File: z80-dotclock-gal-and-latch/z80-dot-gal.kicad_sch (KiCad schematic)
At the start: 14 parts, among them J1 Board corner fix, J2 EXP_PORT, J3 GAL_1_9, J4 GAL_11_19, U1 Z80CPU SOCKET, U2 Z80CPU, U3 74LS74, U4 GAL22V10

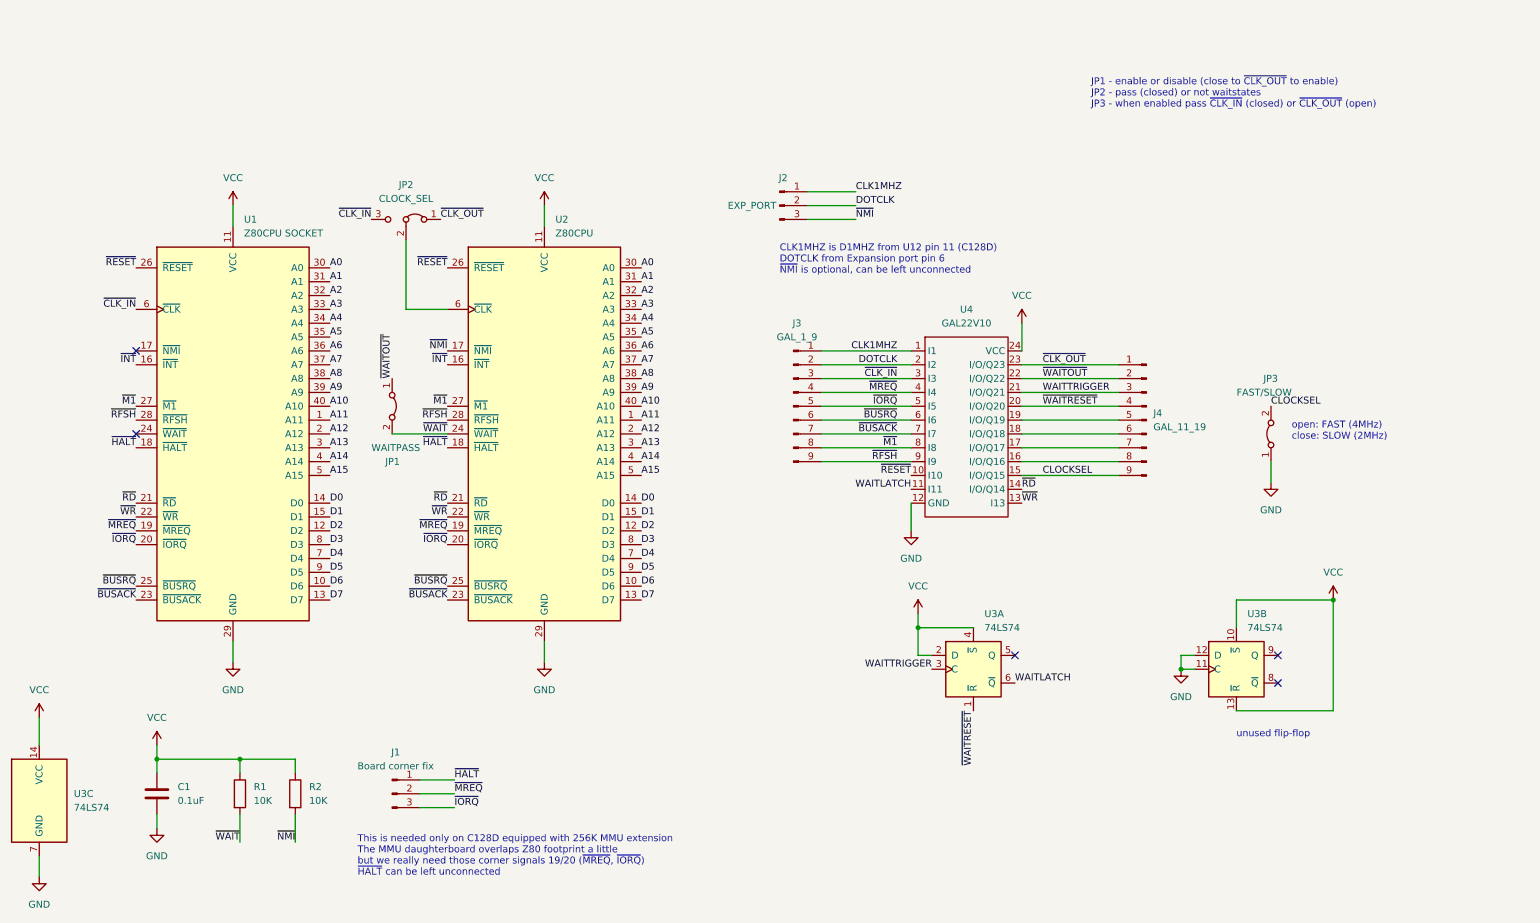
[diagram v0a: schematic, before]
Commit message: Schematic revision v2, without PCB: - remove test pads - remove unused connections to GAL pins 6-8 - add J3 and lots of descriptions - add required connects to /WR, /RESET, /RFSH - make GAL socket compatible with 16V8
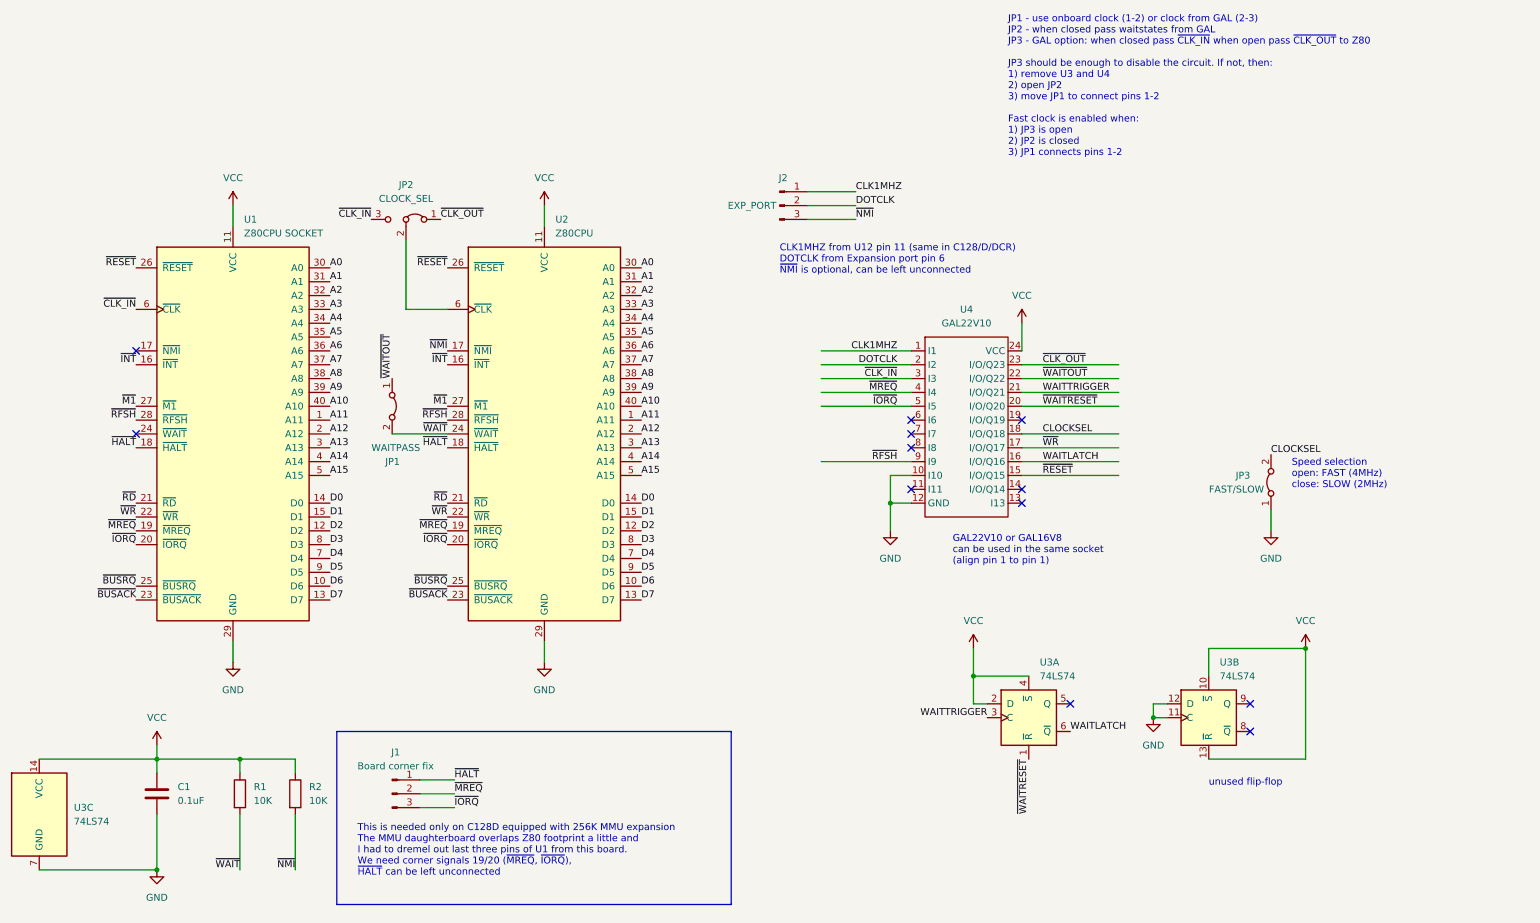
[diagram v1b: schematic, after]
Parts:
- removed J3: GAL_1_9, Connector_PinHeader_2.54mm:PinHeader_1x09_P2.54mm_Vertical, symbol Connector:Conn_01x09_Male
- removed J4: GAL_11_19, Connector_PinHeader_2.54mm:PinHeader_1x09_P2.54mm_Vertical, symbol Connector:Conn_01x09_Male
- U3: footprint (none) -> Package_DIP:DIP-14_W7.62mm_Socket
- U4: footprint (none) -> Package_DIP:DIP-24_W7.62mm_Socket
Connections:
- net CLOCKSEL: now also U4.18 (I/O/Q18); no longer U4.15 (I/O/Q15)
- net GND: now also U4.10 (I10)
- net WAITLATCH: now also U4.16 (I/O/Q16); no longer U4.11 (I11)
- net ~{BUSACK}: no longer U4.7 (I7)
- net ~{BUSRQ}: no longer U4.6 (I6)
- net ~{M1}: no longer U4.8 (I8)
- net ~{RD}: no longer U4.14 (I/O/Q14)
- net ~{RESET}: now also U4.15 (I/O/Q15); no longer U4.10 (I10)
- net ~{WR}: now also U4.17 (I/O/Q17); no longer U4.13 (I13)
- no-connect marks 5 -> 12
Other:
- note added: "CLK1MHZ from U12 pin 11 (same in C128/D/DCR) DOTCLK from Expansion port pin 6 ~{NMI} is optional, can be left unconnected"
- note added: "GAL22V10 or GAL16V8 can be used in the same socket (align pin 1 to pin 1)"
- note added: "JP1 - use onboard clock (1-2) or clock from GAL (2-3) JP2 - when closed pass waitstates from GAL JP3 - GAL option: when closed pass ~{CLK_IN} when open pass ~{CLK_OUT} to Z80 JP3 should be enough to disable the circuit. If not, then: 1) remove U3 and U4 2) open JP2 3) move JP1 to connect pins 1-2 Fast clock is enabled when: 1) JP3 is open 2) JP2 is closed 3) JP1 connects pins 1-2"
- note added: "Speed selection open: FAST (4MHz) close: SLOW (2MHz)"
- note added: "This is needed only on C128D equipped with 256K MMU expansion The MMU daughterboard overlaps Z80 footprint a little and I had to dremel out last three pins of U1 from this board. We need corner signals 19/20 (~{MREQ}, ~{IORQ}), ~{HALT} can be left unconnected"
- note removed: "CLK1MHZ is D1MHZ from U12 pin 11 (C128D) DOTCLK from Expansion port pin 6 ~{NMI} is optional, can be left unconnected"
- note removed: "JP1 - enable or disable (close to ~{CLK_OUT} to enable) JP2 - pass (closed) or not waitstates JP3 - when enabled pass ~{CLK_IN} (closed) or ~{CLK_OUT} (open)"
- note removed: "This is needed only on C128D equipped with 256K MMU extension The MMU daughterboard overlaps Z80 footprint a little but we really need those corner signals 19/20 (~{MREQ}, ~{IORQ}) ~{HALT} can be left unconnected"
- note removed: "open: FAST (4MHz) close: SLOW (2MHz)"
- moved on the sheet: JP3, U3A, U3B, U3C

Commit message: correct descriptions
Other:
- note added: "JP1 - when closed pass waitstates from GAL JP2 - use onboard clock (1-2) or clock from GAL (2-3) JP3 - GAL option: when closed pass ~{CLK_IN} when open pass ~{CLK_OUT} to Z80 JP3 should be enough to disable the circuit. If not, then: 1) remove U3 and U4 2) move JP2 to connect pins 1-2 3) open JP1 Fast clock is enabled when: 1) JP3 is open 2) JP2 connects pins 1-2 3) JP1 is closed"
- note removed: "JP1 - use onboard clock (1-2) or clock from GAL (2-3) JP2 - when closed pass waitstates from GAL JP3 - GAL option: when closed pass ~{CLK_IN} when open pass ~{CLK_OUT} to Z80 JP3 should be enough to disable the circuit. If not, then: 1) remove U3 and U4 2) open JP2 3) move JP1 to connect pins 1-2 Fast clock is enabled when: 1) JP3 is open 2) JP2 is closed 3) JP1 connects pins 1-2"
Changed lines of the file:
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@@
     (effects (font (size 1.27 1.27)) (justify left bottom))
   )
-  (text "JP1 - use onboard clock (1-2) or clock from GAL (2-3)\nJP2 - when closed pass waitstates from GAL\nJP3 - GAL option: when closed pass ~{CLK_IN} when open pass ~{CLK_OUT} to Z80\n\nJP3 should be enough to disable the circuit. If not, then:\n1) remove U3 and U4\n2) open JP2\n3) move JP1 to connect pins 1-2\n\nFast clock is enabled when:\n1) JP3 is open\n2) JP2 is closed\n3) JP1 connects pins 1-2\n"
+  (text "JP1 - when closed pass waitstates from GAL\nJP2 - use onboard clock (1-2) or clock from GAL (2-3)\nJP3 - GAL option: when closed pass ~{CLK_IN} when open pass ~{CLK_OUT} to Z80\n\nJP3 should be enough to disable the circuit. If not, then:\n1) remove U3 and U4\n2) move JP2 to connect pins 1-2\n3) open JP1\n\nFast clock is enabled when:\n1) JP3 is open\n2) JP2 connects pins 1-2\n3) JP1 is closed\n"
     (at 201.93 41.91 0)
     (effects (font (size 1.27 1.27)) (justify left bottom))

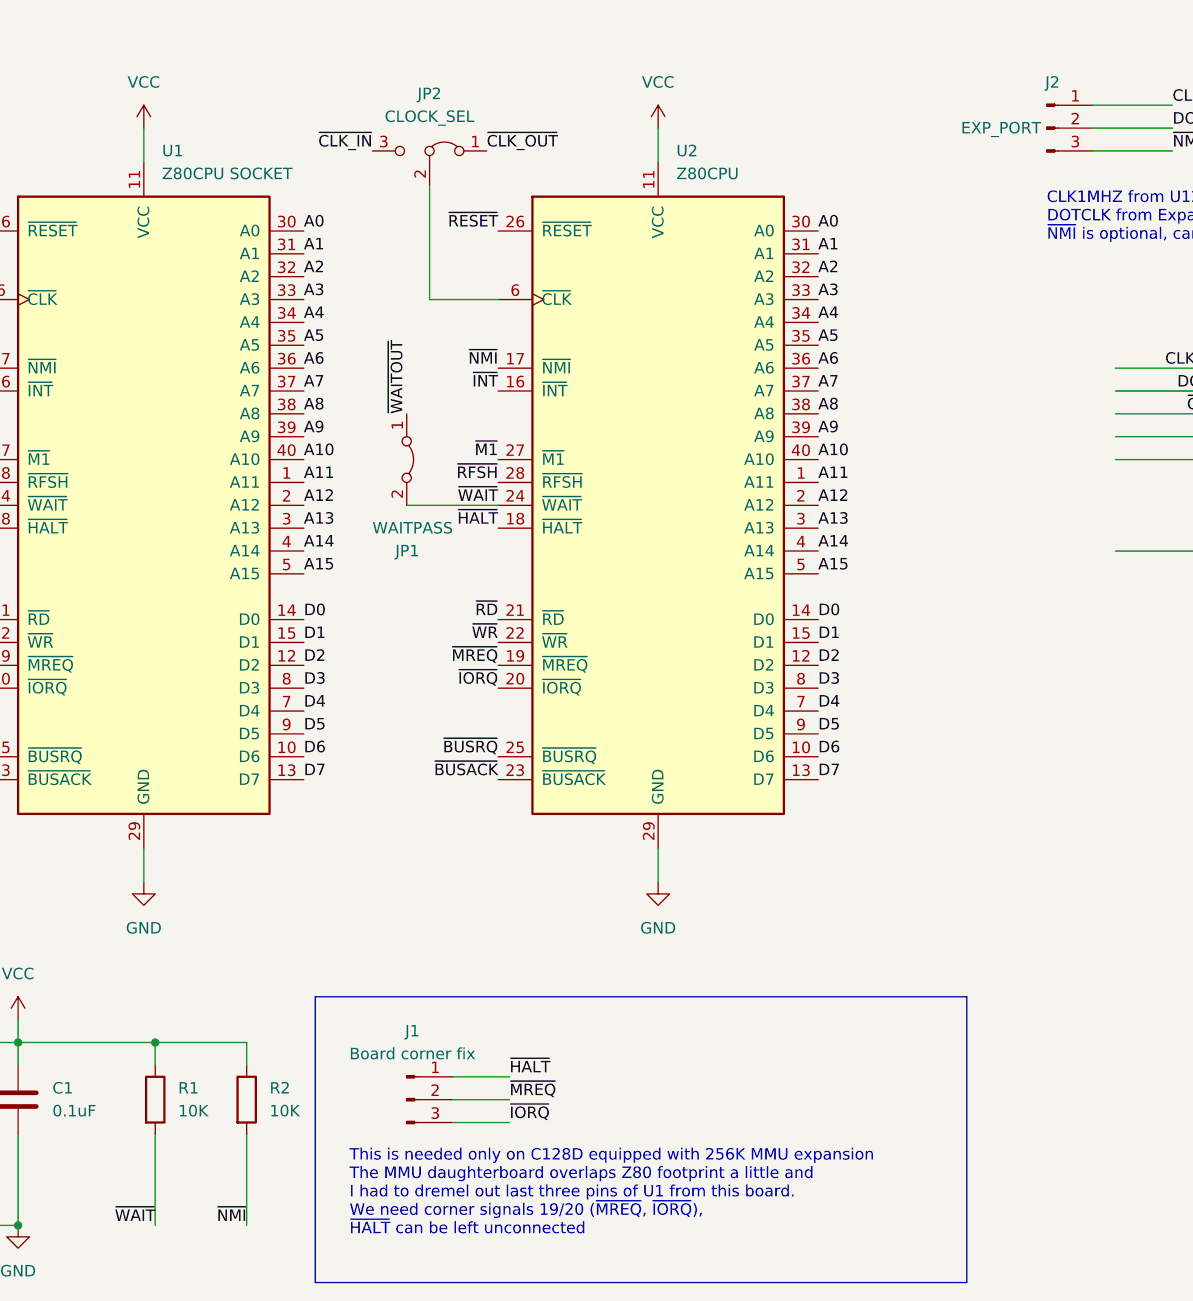
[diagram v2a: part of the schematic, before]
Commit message: C128D/DCR PCB project (without cutout for 256k MMU expansion)
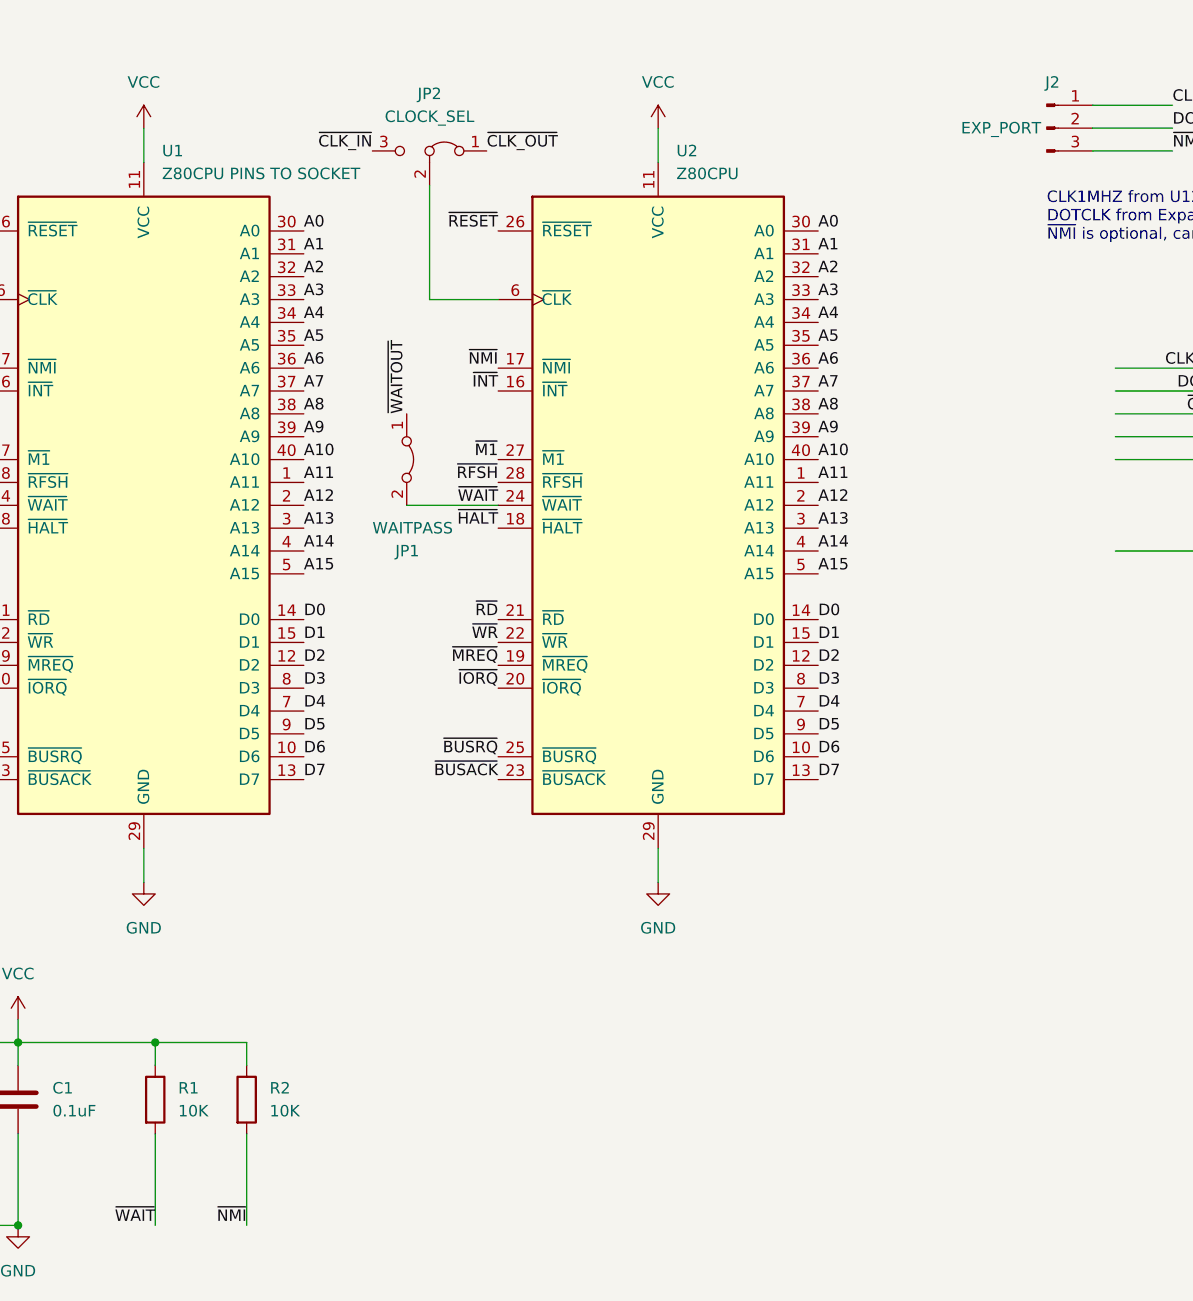
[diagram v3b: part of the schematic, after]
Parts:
- removed J1: Board corner fix, Connector_PinHeader_2.54mm:PinHeader_1x03_P2.54mm_Vertical, symbol Connector:Conn_01x03_Male
- U1: value Z80CPU SOCKET -> Z80CPU PINS TO SOCKET
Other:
- note removed: "This is needed only on C128D equipped with 256K MMU expansion The MMU daughterboard overlaps Z80 footprint a little and I had to dremel out last three pins of U1 from this board. We need corner signals 19/20 (~{MREQ}, ~{IORQ}), ~{HALT} can be left unconnected"
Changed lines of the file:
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@@
-    (stroke (width 0) (type default) (color 0 0 0 0))
-  )
-  (polyline (pts (xy 151.13 179.07) (xy 78.74 179.07))
     (stroke (width 0) (type default) (color 0 0 0 0))
   )
@@
     (stroke (width 0) (type default) (color 0 0 0 0))
   )
-  (polyline (pts (xy 78.74 147.32) (xy 78.74 179.07))
-    (stroke (width 0) (type default) (color 0 0 0 0))
-  )
   (wire (pts (xy 256.54 152.4) (xy 256.54 132.08))
     (stroke (width 0) (type default) (color 0 0 0 0))
   )
-  (wire (pts (xy 93.98 161.29) (xy 100.33 161.29))
-    (stroke (width 0) (type default) (color 0 0 0 0))
-  )
   (wire (pts (xy 180.34 105.41) (xy 184.15 105.41))
     (stroke (width 0) (type default) (color 0 0 0 0))
   )
-  (polyline (pts (xy 78.74 147.32) (xy 151.13 147.32))
-    (stroke (width 0) (type default) (color 0 0 0 0))
-  )
   (wire (pts (xy 59.69 130.81) (xy 59.69 134.62))
     (stroke (width 0) (type default) (color 0 0 0 0))
@@
     (stroke (width 0) (type default) (color 0 0 0 0))
   )
-  (wire (pts (xy 93.98 156.21) (xy 100.33 156.21))
-    (stroke (width 0) (type default) (color 0 0 0 0))
-  )
   (wire (pts (xy 204.47 80.01) (xy 222.25 80.01))
     (stroke (width 0) (type default) (color 0 0 0 0))
@@
     (stroke (width 0) (type default) (color 0 0 0 0))
   )
-  (polyline (pts (xy 151.13 147.32) (xy 151.13 179.07))
-    (stroke (width 0) (type default) (color 0 0 0 0))
-  )
   (wire (pts (xy 91.44 69.85) (xy 99.06 69.85))
     (stroke (width 0) (type default) (color 0 0 0 0))
@@
   )
   (wire (pts (xy 238.76 132.08) (xy 256.54 132.08))
-    (stroke (width 0) (type default) (color 0 0 0 0))
-  )
-  (wire (pts (xy 93.98 158.75) (xy 100.33 158.75))
     (stroke (width 0) (type default) (color 0 0 0 0))
   )
@@
     (effects (font (size 1.27 1.27)) (justify left bottom))
   )
-  (text "This is needed only on C128D equipped with 256K MMU expansion\nThe MMU daughterboard overlaps Z80 footprint a little and\nI had to dremel out last three pins of U1 from this board.\nWe need corner signals 19/20 (~{MREQ}, ~{IORQ}),\n~{HALT} can be left unconnected"
-    (at 82.55 173.99 0)
-    (effects (font (size 1.27 1.27)) (justify left bottom))
-  )
   (text "JP1 - when closed pass waitstates from GAL\nJP2 - use onboard clock (1-2) or clock from GAL (2-3)\nJP3 - GAL option: when closed pass ~{CLK_IN} when open pass ~{CLK_OUT} to Z80\n\nJP3 should be enough to disable the circuit. If not, then:\n1) remove U3 and U4\n2) move JP2 to connect pins 1-2\n3) open JP1\n\nFast clock is enabled when:\n1) JP3 is open\n2) JP2 connects pins 1-2\n3) JP1 is closed\n"
     (at 201.93 41.91 0)
@@
     (effects (font (size 1.27 1.27)) (justify left bottom))
   )
-  (label "~{IORQ}" (at 100.33 161.29 0)
-    (effects (font (size 1.27 1.27)) (justify left bottom))
-  )
   (label "~{RD}" (at 41.91 105.41 180)
     (effects (font (size 1.27 1.27)) (justify right bottom))
@@
     (effects (font (size 1.27 1.27)) (justify right bottom))
   )
-  (label "~{HALT}" (at 100.33 156.21 0)
-    (effects (font (size 1.27 1.27)) (justify left bottom))
-  )
   (label "~{WAITRESET}" (at 208.28 87.63 0)
     (effects (font (size 1.27 1.27)) (justify left bottom))
@@
     (effects (font (size 1.27 1.27)) (justify right bottom))
   )
-  (label "~{MREQ}" (at 100.33 158.75 0)
-    (effects (font (size 1.27 1.27)) (justify left bottom))
-  )
   (label "D4" (at 134.62 115.57 0)
     (effects (font (size 1.27 1.27)) (justify left bottom))
@@
   (label "A3" (at 134.62 69.85 0)
     (effects (font (size 1.27 1.27)) (justify left bottom))
-  )
-  (symbol (lib_id "Connector:Conn_01x03_Male") (at 88.9 158.75 0) (unit 1)
-    (in_bom yes) (on_board yes) (fields_autoplaced)
-    (property "Reference" "J1" (id 0) (at 89.535 151.13 0))
-    (property "Value" "Board corner fix" (id 1) (at 89.535 153.67 0))
-    (property "Footprint" "Connector_PinHeader_2.54mm:PinHeader_1x03_P2.54mm_Vertical" (id 2) (at 88.9 158.75 0)
-      (effects (font (size 1.27 1.27)) hide)
-    )
-    (property "Datasheet" "~" (id 3) (at 88.9 158.75 0)
-      (effects (font (size 1.27 1.27)) hide)
-    )
-    (pin "1")
-    (pin "2")
-    (pin "3")
   )
   (symbol (lib_id "power:GND") (at 228.6 144.78 0) (unit 1)
@@
       (effects (font (size 1.27 1.27)) (justify left))
     )
-    (property "Value" "Z80CPU SOCKET" (id 1) (at 61.7094 55.88 0)
+    (property "Value" "Z80CPU PINS TO SOCKET" (id 1) (at 61.7094 55.88 0)
       (effects (font (size 1.27 1.27)) (justify left))
     )
@@
       (reference "C1") (unit 1) (value "0.1uF") (footprint "Capacitor_THT:C_Disc_D8.0mm_W2.5mm_P5.00mm")
     )
-    (path "/097f5502-6711-4937-a2d7-da17dd154a4f"
-      (reference "J1") (unit 1) (value "Board corner fix") (footprint "Connector_PinHeader_2.54mm:PinHeader_1x03_P2.54mm_Vertical")
-    )
     (path "/eb66d20f-5ca8-4787-a518-39b01f9bb9ca"
       (reference "J2") (unit 1) (value "EXP_PORT") (footprint "Connector_PinHeader_2.54mm:PinHeader_1x03_P2.54mm_Vertical")
@@
     )
     (path "/2029b3a6-9e22-4efd-a71e-a068838d38a5"
-      (reference "U1") (unit 1) (value "Z80CPU SOCKET") (footprint "Package_DIP:DIP-40_W15.24mm_Socket_LongPads")
+      (reference "U1") (unit 1) (value "Z80CPU PINS TO SOCKET") (footprint "Package_DIP:DIP-40_W15.24mm_Socket_LongPads")
     )
     (path "/abc4f9b8-c27f-475b-bf9d-5f9c132bd2e2"
